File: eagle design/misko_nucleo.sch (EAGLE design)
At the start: 54 parts, among them CN1 LiPo Battery, IC1 TPS63031, IC2 RN4678_BT_MODULE, IC3 MAX6818, Q1 BSS84, SW1 MICROJOYSTICK, SW2 PB6156RSL, SW3 PB6156RSL, U1 SN74LVC1G3157DBVR - BT switch, U2 ATMEGA1281-16AU, U3 MCP73871-2AAI/ML, U4 SN74LVC1G3157DBVR - GPS switch, X1 FH12-30S-0.5SH

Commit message: in brd & sch/misko.ioc/main.c/.h: - added support for a supercap discharge FET/resistor circuit
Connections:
- net PC1 renamed SUPERCAP_DISCHARGE
- net N$1: now also R1.1
- net VOUT: now also R1.2
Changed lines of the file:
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@@
 <port name="VOUT" side="right" coord="0" direction="pwr"/>
 <port name="!EN!" side="left" coord="-5.08" direction="in"/>
+<port name="SC_DIS" side="bottom" coord="-7.62" direction="in"/>
 </ports>
 <variantdefs>
@@
 <part name="SUPPLY1" library="Power_Symbols" library_urn="urn:adsk.eagle:library:16502351" deviceset="GND-BAR" device="" value="GND"/>
 <part name="SUPPLY2" library="Power_Symbols" library_urn="urn:adsk.eagle:library:16502351" deviceset="3V3-CIRCLE" device="" value="3V3"/>
+<part name="R1" library="resistor" library_urn="urn:adsk.eagle:library:348" deviceset="R-EU_" device="R1206" package3d_urn="urn:adsk.eagle:package:26062/1" value="33R"/>
+<part name="Q4" library="transistor-small-signal" library_urn="urn:adsk.eagle:library:401" deviceset="BSS123" device="" package3d_urn="urn:adsk.eagle:package:28738/2" value="SQ2310ES-T1_BE3"/>
+<part name="SUPPLY3" library="Power_Symbols" library_urn="urn:adsk.eagle:library:16502351" deviceset="GND-BAR" device="" value="GND"/>
 </parts>
 <sheets>
@@
 <attribute name="VALUE" x="66.04" y="27.94" size="1.778" layer="96" align="center-left"/>
 </instance>
+<instance part="R1" gate="G$1" x="165.1" y="88.9" smashed="yes" rot="R90">
+<attribute name="NAME" x="167.64" y="88.9" size="1.778" layer="95"/>
+<attribute name="VALUE" x="167.64" y="86.36" size="1.778" layer="96"/>
+</instance>
+<instance part="Q4" gate="G$1" x="165.1" y="53.34" smashed="yes">
+<attribute name="NAME" x="167.64" y="53.34" size="1.778" layer="95"/>
+<attribute name="VALUE" x="162.56" y="48.26" size="1.778" layer="96" rot="R180"/>
+</instance>
+<instance part="SUPPLY3" gate="G$1" x="165.1" y="43.18" smashed="yes">
+<attribute name="VALUE" x="165.1" y="40.64" size="1.778" layer="96" align="center-left"/>
+</instance>
 </instances>
 <busses>
@@
 <label x="76.2" y="22.86" size="1.778" layer="95" xref="yes"/>
 </segment>
+<segment>
+<pinref part="Q4" gate="G$1" pin="S"/>
+<pinref part="SUPPLY3" gate="G$1" pin="GND"/>
+<wire x1="165.1" y1="45.72" x2="165.1" y2="48.26" width="0.1524" layer="91"/>
+</segment>
 </net>
 <net name="!EN!" class="2">
@@
 <segment>
 <pinref part="C24" gate="G$1" pin="+"/>
-<wire x1="149.86" y1="93.98" x2="160.02" y2="93.98" width="0.1524" layer="91"/>
-<label x="160.02" y="93.98" size="1.778" layer="95"/>
+<wire x1="149.86" y1="93.98" x2="165.1" y2="93.98" width="0.1524" layer="91"/>
+<label x="172.72" y="93.98" size="1.778" layer="95"/>
+<wire x1="165.1" y1="93.98" x2="172.72" y2="93.98" width="0.1524" layer="91"/>
 <wire x1="149.86" y1="93.98" x2="124.46" y2="93.98" width="0.1524" layer="91"/>
 <junction x="149.86" y="93.98"/>
@@
 <junction x="124.46" y="93.98"/>
 <label x="106.68" y="93.98" size="1.778" layer="95"/>
+<pinref part="R1" gate="G$1" pin="2"/>
+<junction x="165.1" y="93.98"/>
 </segment>
 </net>
@@
 </segment>
 </net>
+<net name="N$1" class="2">
+<segment>
+<pinref part="Q4" gate="G$1" pin="D"/>
+<pinref part="R1" gate="G$1" pin="1"/>
+<wire x1="165.1" y1="58.42" x2="165.1" y2="83.82" width="0.1524" layer="91"/>
+</segment>
+</net>
+<net name="SC_DIS" class="0">
+<segment>
+<pinref part="Q4" gate="G$1" pin="G"/>
+<wire x1="160.02" y1="50.8" x2="137.16" y2="50.8" width="0.1524" layer="91"/>
+<label x="137.16" y="50.8" size="1.778" layer="95" rot="R180" xref="yes"/>
+</segment>
+</net>
 </nets>
 </sheet>
@@
 <port name="!RESET!" side="left" coord="-7.62" direction="in"/>
 <port name="SC_!EN!" side="left" coord="-12.7" direction="in"/>
+<port name="SC_DIS" side="left" coord="-10.16" direction="in"/>
 </ports>
 <variantdefs>
@@
 </segment>
 </net>
+<net name="SC_DIS" class="0">
+<segment>
+<portref moduleinst="SUPERCAP+CHARGER" port="SC_DIS"/>
+<wire x1="96.52" y1="48.26" x2="96.52" y2="40.64" width="0.1524" layer="91"/>
+<wire x1="96.52" y1="40.64" x2="40.64" y2="40.64" width="0.1524" layer="91"/>
+<wire x1="40.64" y1="40.64" x2="40.64" y2="144.78" width="0.1524" layer="91"/>
+<label x="40.64" y="144.78" size="1.778" layer="95" rot="R90" xref="yes"/>
+</segment>
+</net>
 </nets>
 </sheet>
@@
 </segment>
 </net>
-<net name="PC1" class="2">
-<segment>
-<wire x1="43.18" y1="180.34" x2="33.02" y2="180.34" width="0.1524" layer="91"/>
-<pinref part="BRD1" gate="CN7" pin="PC1"/>
-<label x="33.02" y="180.34" size="1.778" layer="95" rot="R180"/>
-</segment>
-</net>
 <net name="LED_YELLOW" class="2">
 <segment>
@@
 </segment>
 </net>
+<net name="SUPERCAP_DISCHARGE" class="0">
+<segment>
+<portref moduleinst="GPS" port="SC_DIS"/>
+<wire x1="325.12" y1="195.58" x2="314.96" y2="195.58" width="0.1524" layer="91"/>
+<label x="314.96" y="195.58" size="1.778" layer="95" rot="R180"/>
+</segment>
+<segment>
+<wire x1="43.18" y1="180.34" x2="33.02" y2="180.34" width="0.1524" layer="91"/>
+<pinref part="BRD1" gate="CN7" pin="PC1"/>
+<label x="33.02" y="180.34" size="1.778" layer="95" rot="R180"/>
+</segment>
+</net>

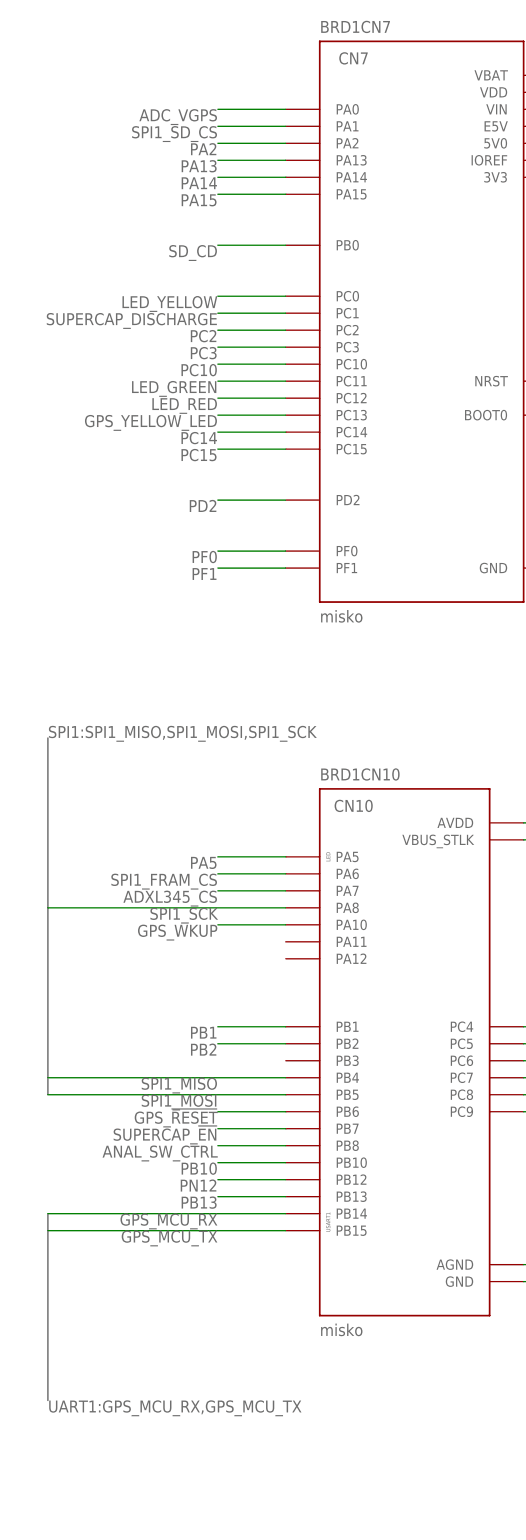
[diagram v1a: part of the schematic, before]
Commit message: in misko.ioc: - moved SPI1_SD_CS from PA1 to PA2 - added timer2 rotary encoder GPIOs on PA1 and PB2 - added I2C2 in DMA mode
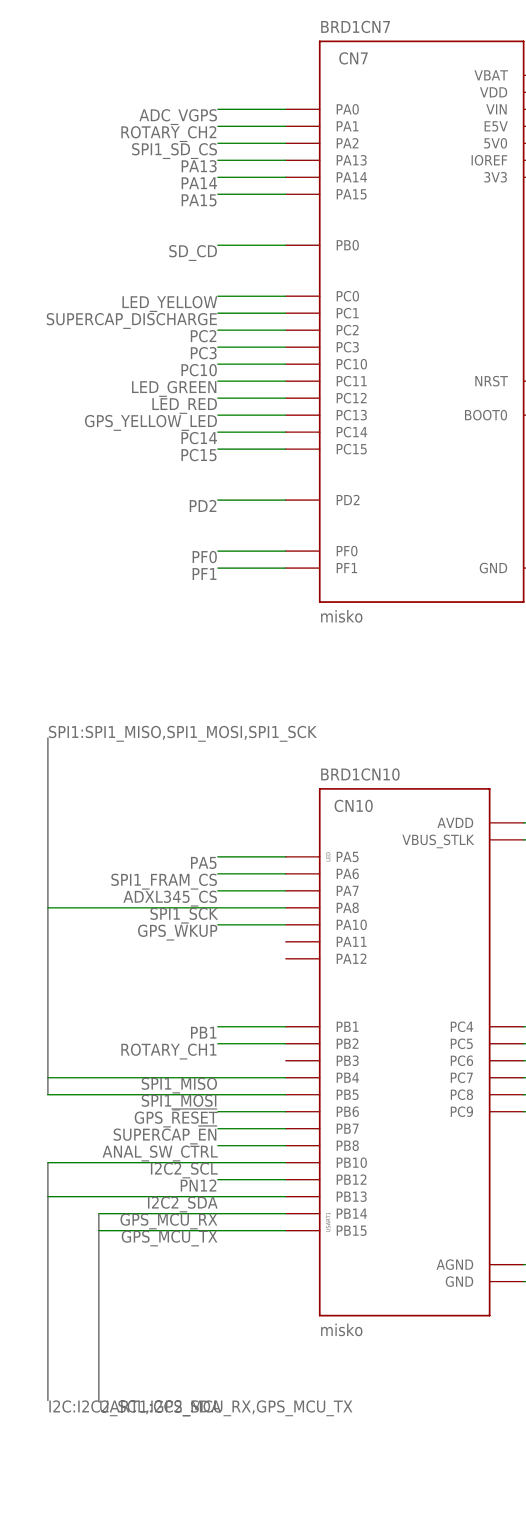
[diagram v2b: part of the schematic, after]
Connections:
- net PB10 renamed I2C2_SCL
- net PB13 renamed I2C2_SDA
- net PB2 renamed ROTARY_CH1
- removed net PA2: BRD1CN7.PA2
- new net ROTARY_CH2: BRD1CN7.PA1
- net SPI1_SD_CS: now also BRD1CN7.PA2; no longer BRD1CN7.PA1

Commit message: in sch & brd: - changed hierarchical module names so that board components have shorter names (GPS subsystem stuff) - added CAN infra. components to sch
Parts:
- removed C1, C10, C13, C8: 10µF, rcl:C-EUC0805
- removed C11, C14: 10µF, resistor:C-EUC0805
- removed C12: 1000µF, rcl:CPOL-EUE5-10.5
- removed C2: 0.1µF, rcl:C-EUC0805
- removed C3, C4, C6, C7: 1µF, rcl:C-EUC0805
- removed C5: 22µF, rcl:C-EUC0805
- removed C9: 2.2µF / 25V, rcl:C-EUC0805
- removed CN1: LiPo Battery, SIM800C:JST_2PIN-THM-RA
- removed D1: BZG05C3V6-E3-TR3, zener:ZENER
- removed D2: SZ1SMB5916BT3G, diode:DIODE-SMB
- removed D3: BAT60AE6327, diode:BAT60J
- removed IC1: TPS63031, TPS63031 - Buck Boost Voltage Regulator:TPS63001DRCR
- removed IC2: RN4678_BT_MODULE, RN4678 Bluetooth 4.2 Dual Mode:RN4678_BT_MODULE
- removed IC3: MAX6818, MAX6818 CMOS Switch debouncer:MAX6818
- removed L1: DJNR3015-1R5, DJNR3015-1R5 Inductor:DJNR3015-1R5
- removed Q1: BSS84, transistor-small-signal:BSS84
- removed R1, R10, R12, R13, R9: 10k, resistor:R-EU_R0805
- removed R11, R6: 1k, resistor:R-EU_R0805
- removed R14, R15: 1k, rcl:R-EU_R0805
- removed R16, R2: 100k, rcl:R-EU_R0805
- removed R17, R3: 270k, rcl:R-EU_R0805
- removed R18: NTC 10k, rcl:R-EU_0204/5
- removed R19, R20: 150k, rcl:R-EU_R0805
- removed R4, R5, R7: 47k, rcl:R-EU_R0805
- removed R8: 390k, rcl:R-EU_R0805
- removed S1: POWER SWITCH, smd-special:SWS001
- removed SJ1: RESET, jumper:SJW
- removed SW1: MICROJOYSTICK, micro joystick:MICROJOYSTICK
- removed SW2, SW3: PB6156RSL, PB6156RSL Illuminated Tact SPST-NO switch:PB6156RSL
- removed U1: SN74LVC1G3157DBVR - BT switch, Texas Instruments_By_element14_Batch_1:SN74LVC1G3157DBVR
- removed U2: ATMEGA1281-16AU, Atmel_By_element14_Batch_1-00:ATMEGA1281-16AU
- removed U3: MCP73871-2AAI/ML, MCP73871 - Powerpath and Charge Controller:MCP73871-2AAI/ML
- removed U4: SN74LVC1G3157DBVR - GPS switch, Texas Instruments_By_element14_Batch_1:SN74LVC1G3157DBVR
- removed X1: FH12-30S-0.5SH, con-hirose:FH12-30S-0.5SH
- added J1: CAN, con-amp:MTA02-100
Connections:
- net PN12 renamed CAN_!STBY!
- removed net !EN!: IC2.EN
- removed net !MR!: IC2.!MR!
- removed net !RESET!: IC1.!RESET!, IC2.!RESET!, R18.1
- removed net ADXL345SDA: IC1.SDA, IC2.Y
- removed net ADXL345_INT1_INTERRUPT_PIN: U2.(SCL/INT0)_PD0
- removed net ADXL345_INT2: IC1.INT2
- removed net ANALOG_SW_CTRL_PIN: U1.S, U2.PA7_(AD7), U4.S
- removed net AREF: U2.AREF
- removed net AVCC: U2.AVCC
- removed net BAT_A_PIN: R19.2, R20.1, U2.PF2_(ADC2)
- removed net BLUETOOTH_PROF_IND_PIN: IC2.P0_5, U2.PG2_(ALE)
- removed net BLUETOOTH_RX: IC2.RXD, U1.A
- removed net BLUETOOTH_SWITCH_PIN: IC2.SW_BTN, R13.2, U2.PC6_(A14)
- removed net BLUETOOTH_TX: IC2.TXD, U4.B1
- removed net BLUETOOTH_WAKEUP_PIN: IC2.WAKEUP, R12.2, U2.PC7_(A15)
- removed net BT_LED: IC2.LED, R6.1
- removed net BUTTON_BLUETOOTH: IC3.IN7, SW3.3
- removed net BUTTON_CENTER: IC3.IN5, SW1.CENTER
- removed net BUTTON_DOWN: IC3.IN2, SW1.DOWN
- removed net BUTTON_GPRS: IC3.IN8, SW2.3
- removed net BUTTON_LEFT: IC3.IN4, SW1.LEFT
- removed net BUTTON_RIGHT: IC3.IN3, SW1.RIGHT
- removed net BUTTON_UP: IC3.IN6, SW1.UP
- removed net CAP1N: C3.1, X1-5.1
- removed net CAP1P: C3.2, X1-4.1
- removed net CAP2N: C4.1, X1-3.1
- removed net CAP2P: C4.2, X1-2.1
- removed net CT: IC2.CT
- removed net EN: IC1.EN, R1.2, S1.1
- removed net FORCE-ON: IC1.FORCE-ON
- removed net FRAM_!HOLD!: IC1.!HOLD!
- removed net FRAM_!WP!: IC1.!WP!
- removed net GPRS_NETLIGHT: R10.1, R9.1
- removed net GPRS_NETLIGHT_GATE: Q1.G, R10.2
- removed net GPS_GREEN_LED_PIN: U2.PA3_(AD3)
- removed net GPS_POWER_CTL_PIN: U2.PA6_(AD6)
- removed net GPS_RED_LED_PIN: U2.PA4_(AD4)
- removed net GPS_RX: IC1.RX, R2.2
- removed net GPS_SW_SERIAL_RX: U1.B2, U2.(OC2A/_PCINT4)_PB4, U4.A
- removed net GPS_TX: IC1.TX, R1.2
- removed net GPS_WAKEUP_PIN: U2.PA5_(AD5)
- removed net GREEN: Q1.G
- removed net G_A: Q1.D
- removed net G_C: R3.1
- removed net IREF: R8.2, X1-26.1
- removed net JTAG_TCL_PIN: U2.PF4_(ADC4/TCK)
- removed net JTAG_TDI_PIN: U2.PF7_(ADC7/TDI)
- removed net JTAG_TDO_PIN: U2.PF6_(ADC6/TDO)
- removed net JTAG_TMS_PIN: U2.PF5_(ADC5/TMS)
- removed net L2: R6.2, SW3.L2
- removed net LDO33_O: IC2.LDO33_O, IC2.VDD_IO, SW3.L1
- removed net L_L1: IC1.L1, L1.L1
- removed net L_L2: IC1.L2, L1.L2
- removed net MCP73871_CHARGE_STATUS_1_PIN: R7.2, U2.PA0_(AD0), U3.STAT1/!LBO!
- removed net MCP73871_CHARGE_STATUS_2_PIN: R5.2, U2.PA1_(AD1), U3.STAT2
- removed net MCP73871_POWER_GOOD_PIN: R4.2, U2.PA2_(AD2), U3.!PG!
- removed net MENU_BLUETOOTH_POWER_BUTTON_PIN: IC3.OUT7, U2.PC4_(A12)
- removed net MENU_CENTER_BUTTON_PIN: IC3.OUT5, U2.PC2_(A10)
- removed net MENU_DOWN_BUTTON_PIN: IC3.OUT2, U2.PG1_(~RD)
- removed net MENU_GPRS_POWER_BUTTON_PIN: IC3.OUT8, U2.PC5_(A13)
- removed net MENU_LEFT_BUTTON_PIN: IC3.OUT4, U2.PC1_(A9)
- removed net MENU_RIGHT_BUTTON_PIN: IC3.OUT3, U2.PC0_(A8)
- removed net MENU_UP_BUTTON_PIN: IC3.OUT6, U2.PC3_(A11)
- removed net N$1: R1.1, R11.1, SW2.L2
- removed net N$11: IC2.!RST_N!, SJ1.1
- removed net N$19: R14.2, R17.1, R18.1
- removed net N$3: Q1.S, R11.2
- removed net N$6: C12.+, D3.C
- removed net OLD_5V0: D3.A, R2.1, U3.!TE!, U3.CE, U3.IN1, U3.IN2, U3.PROG2, U3.SEL
- removed net PDI_UART0_CTS_PIN: U2.(OC0B)_PG5
- removed net PDI_UART0_RX_PIN: U2.(RXD0/PCINT8/PDI)_PE0
- removed net PDI_UART0_TX_PIN: U2.(TXD0/PDO)_PE1
- removed net PFI: IC2.PFI
- removed net PFI_RET: IC2.PFI_RET
- removed net PROG: IC2.PROG, R14.2
- removed net PROG1: R15.1, U3.PROG1
- removed net PROG3: R16.1, U3.PROG3
- removed net RESET: U2.~RESET
- removed net RTC_INT_INTERRUPT_PIN: U2.(SDA/INT1)_PD1
- removed net RX: R2.1
- removed net R_C: R1.1
- removed net SD_CARD_DETECT_PIN: U2.(XCK0/AIN0)_PE2
- removed net SENSE: C1.1, IC2.SENSE
- removed net SPI_MISO_PIN: U2.(MISO/PCINT3)_PB3
- removed net SPI_MOSI_PIN: U2.(MOSI/PCINT2)_PB2, X1-19.1
- removed net SPI_OLED_D/C_PIN: U2.(OC0A/OC1C/PCINT7)_PB7, X1-15.1
- removed net SPI_OLED_RESET_PIN: U2.(TOSC2)_PG3, X1-14.1
- removed net SPI_SCK_PIN: U2.(SCK/PCINT1)_PB1, X1-18.1
- removed net SPI_SS_ADXL345_PIN: U2.(OC1B/PCINT6)_PB6
- removed net SPI_SS_FRAM_PIN: U2.(~SS/PCINT0)_PB0
- removed net SPI_SS_OLED_PIN: U2.(TOSC1)_PG4, X1-13.1
- removed net SPI_SS_RTC_PIN: U2.(OC3C/INT5)_PE5
- removed net SPI_SS_SD_CARD_PIN: U2.(OC3A/AIN1)_PE3
- removed net THERM: R14.1, U3.THERM
- removed net TMP36_VSENSE_PIN: U2.PF3_(ADC3)
- removed net TX: R1.1
- removed net UART1_GPS_RX: U2.(RXD1/INT2)_PD2
- removed net UART1_GPS_TX: U2.(TXD1/INT3)_PD3
- removed net VCC: C10.1, C13.1, C5.2, C6.2, C7.2, C8.2, D1.CAT, D2.C, IC1.FB, IC1.VOUT, IC2.BAT_IN, IC3.VCC, R4.1, R5.1, R7.1, U1.VCC, U2.VCC, U2.VCC_2, U4.VCC, X1-28.1, X1-6.1, X1-9.1
- removed net VCC_SENSE_PIN: U2.PF1_(ADC1)
- removed net VCOMH: C9.2, X1-27.1
- removed net VGPS: C1.1, C2.1, IC1.VCC
- removed net VMID: C1.1, IC2.VMID
- removed net VOUT: IC2.VOUT, R1.2
- removed net VPCC: R2.2, R3.1, U3.VPCC
- removed net V_LIION+: C14.1, CN1.2, R19.1, U3.VBAT1, U3.VBAT2, U3.VBAT_SENSE
- removed net V_LIION_REGULATED: C1.2, C11.1, C2.1, IC1.PS/SYNC, IC1.VIN, IC1.VINA, S1.2, SW2.L1, U3.OUT1, U3.OUT2
- removed net WAKEUP: IC1.WAKEUP
- removed net XTAL1: U2.XTAL1
- removed net XTAL2: U2.XTAL2
- removed net Y_C: R2.1
- new net CAN_H: J1.1
- new net CAN_L: J1.2
- net 3V3: no longer C1.1, C2.1, C4.1, IC1.DET, IC1.VCC, IC1.VDD, IC1.VDDIO, IC1.VS, IC2.FB, IC2.SEL, IC2.VCC, IC2.VDD, IC2.VIN, R1.2, R18.2, R2.2, R3.2
- net ADXL345_CS: no longer IC1.!CS!, IC2.A
- net ADXL345_INT1: no longer IC1.INT1
- net GND: no longer C1.1, C1.2, C10.2, C11.2, C12.-, C13.2, C14.2, C2.2, C4.2, C5.1, C6.1, C7.1, C8.1, C9.1, CN1.1, D1.AN, D2.A, IC1.GND, IC1.PGND, IC1.POWERPAD, IC1.VSS, IC2.GND, IC3.!EN!, IC3.GND, Q1.D, Q1.S, R1.1, R12.1, R13.1, R14.1, R15.2, R16.2, R17.2, R18.2, R20.2, R3.2, R8.1, R9.2, SJ1.2, SW1.GND1, SW1.GND2, SW1.GND3, SW2.1, SW2.GND, SW3.1, SW3.GND, U1.GND, U2.GND, U2.GND_2, U2.GND_3, U3.GND1, U3.GND2, U3.GND3, U3.GND4, U3.GND5, U3.GND6, U4.GND, X1-1.1, X1-10.1, X1-11.1, X1-12.1, X1-29.1, X1-30.1, X1-8.1
- net GPS_MCU_RX: no longer U1.B1, U2.(OC1A/PCINT5)_PB5
- net GPS_MCU_TX: no longer U4.B2
- net SD_CD: no longer IC1.POL
- net SPI1_FRAM_CS: no longer IC1.!CS!
- net SPI1_MISO: no longer IC1.DAT0, IC1.SDO, IC1.SO
- net SPI1_MOSI: no longer IC1.CMD, IC1.SI, IC2.B
- net SPI1_SCK: no longer IC1.CLK, IC1.SCK, IC1.SCL
- net SPI1_SD_CS: no longer IC1.CD/DAT3
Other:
- note added: "GPS"
- note added: "GPS subsystem"
- note added: "internal pulldown"
- note added: "supercap charger"
- note added: "voltage supervisor"
- note removed: "ADXL345 Accelerometer"
- note removed: "Analog Switch"
- note removed: "Bluetooth Module"
- note removed: "Buttons"
- note removed: "Debouncer"
- note removed: "ER-OLED015-2W Connetor w. SSD1309"
- note removed: "FERAM Module"
- note removed: "GPS module"
- note removed: "Joystick"
- note removed: "Motherboard"
- note removed: "OLED"
- note removed: "Power Supply - Buck/Boost Regulator"
- note removed: "Power Supply - Power Path Controller"
- note removed: "RTC Clock"
- note removed: "Reset Circuit"
- note removed: "SD Card Slot"
- note removed: "SPI Bus"
- note removed: "Supercap Charger"
- note removed: "Temperature Sensor"
- note removed: "USB connetor"
- note removed: "USB to Serial"
- note removed: "VGPS Voltage Supervisor"
- note removed: "Vcc Measurement"
- note removed: "Voltage Reference"

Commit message: board rev.3 on nucleo - connected & routed a nucleo H503RB-B02 compatible sch & brd - moved GPIOs to better suited physical locations - added yellow LED - sent board to the fab
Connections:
- net GPS_YELLOW_LED renamed USER_BUTTON
- removed net PA5: BRD1CN10.PA5
- removed net PB1: BRD1CN10.PB1
- removed net PC2: BRD1CN7.PC2
- removed net PC3: BRD1CN7.PC3
- removed net PC5: BRD1CN10.PC5
- new net PA10: BRD1CN10.PA10
- new net PA7: BRD1CN10.PA7
- new net PB0: BRD1CN7.PB0
- new net PB12: BRD1CN10.PB12
- new net PC4: BRD1CN10.PC4
- net ADXL345_CS: now also BRD1CN10.PB6; no longer BRD1CN10.PA7
- net CAN_!STBY!: now also BRD1CN10.PC5; no longer BRD1CN10.PB12
- net GPS_!RESET!: now also BRD1CN7.PC3; no longer BRD1CN10.PB6
- net GPS_PWR_CTRL: now also BRD1CN10.PB1; no longer BRD1CN10.PC4
- net GPS_WKUP: now also BRD1CN7.PC2; no longer BRD1CN10.PA10
- net LED_GREEN: now also BRD1CN10.PA5; no longer BRD1CN7.PC11
- net LED_RED: now also BRD1CN7.PC0; no longer BRD1CN7.PC12
- net LED_YELLOW: now also BRD1CN7.PC1; no longer BRD1CN7.PC0
- net SD_CD: now also BRD1CN7.PC12; no longer BRD1CN7.PB0
- net SUPERCAP_DISCHARGE: now also BRD1CN7.PC11; no longer BRD1CN7.PC1
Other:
- note added: "3.3V"
- note added: "?"
- note added: "free"
- moved on the sheet: J1

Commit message: rev.3a branch
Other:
- note added: "misko POC ejovrh rev.3a"
- note removed: "misko POC ejovrh rev.3"
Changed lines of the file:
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@@
 <plain>
 <text x="304.8" y="12.7" size="1.778" layer="97">misko POC
-ejovrh rev.3</text>
+ejovrh rev.3a</text>
 <text x="350.52" y="231.14" size="1.778" layer="91" align="center">GPS subsystem</text>
 <text x="58.42" y="190.5" size="1.778" layer="97" align="center-left">free</text>
